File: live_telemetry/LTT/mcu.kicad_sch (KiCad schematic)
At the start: 15 parts, among them J1 Programming Header, U1 MC2562, U2 PIC18F26K83, Y1 Crystal

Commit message: started schematic
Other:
- note added: "CAN"
- note added: "Crystal"
- note added: "MCU"
- note added: "Programmable Test LED's"
- note added: "Programming Header"
- note added: "Standard Waterloo Rocketry PIC18 Setup"
- moved on the sheet: C1, C2, C3, C4, D1, D2, D3, J1, R3, R4, R5, R6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

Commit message: completed schematic
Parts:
- renumbered C4 to C2, C2 to C3, C3 to C4, R3 to R1, R4 to R2, R5 to R3, R6 to R4
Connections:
- net SCLK: now reaches U2.14 (RC3)
- net MOSI: now reaches U2.15 (RC4)
- net MISO: now reaches U2.16 (RC5)
- net RESET: now reaches U2.18 (RC7)
- net CURR_AMP_CAN: now reaches U2.2 (RA0)
- net CS: now reaches U2.7 (RA5)
- no-connect marks 4 -> 9
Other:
- note removed: "MCU"
- moved on the sheet: C2, R1, U2

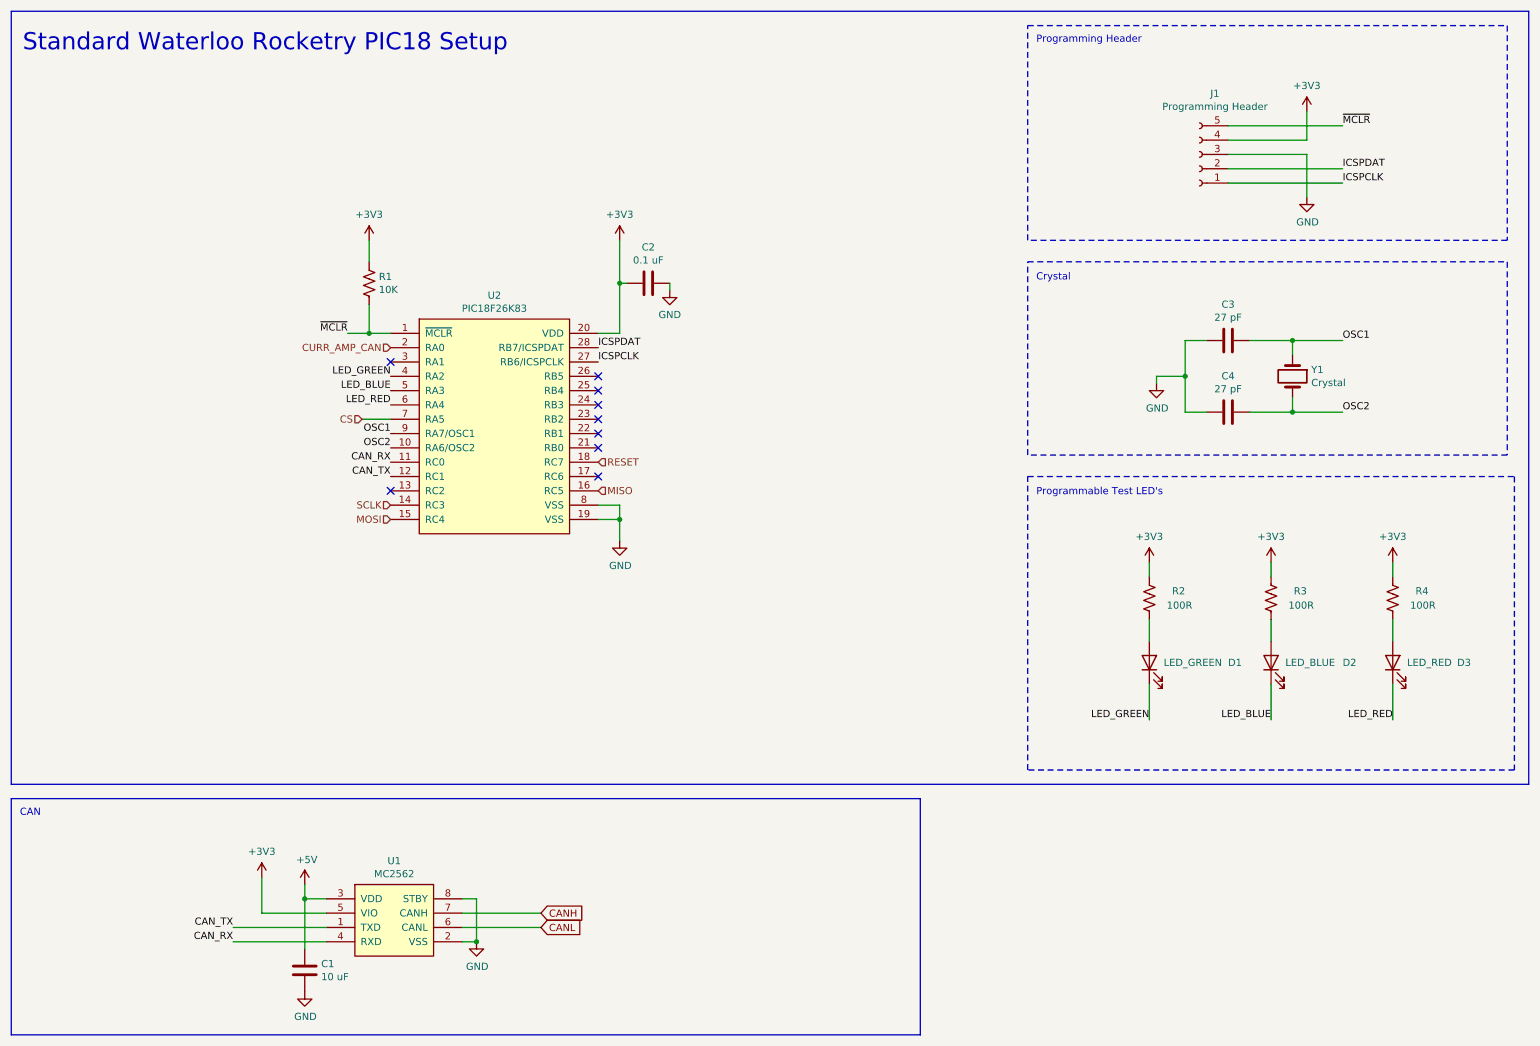
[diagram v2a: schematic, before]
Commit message: switched pic and test led's to 5v from 3v
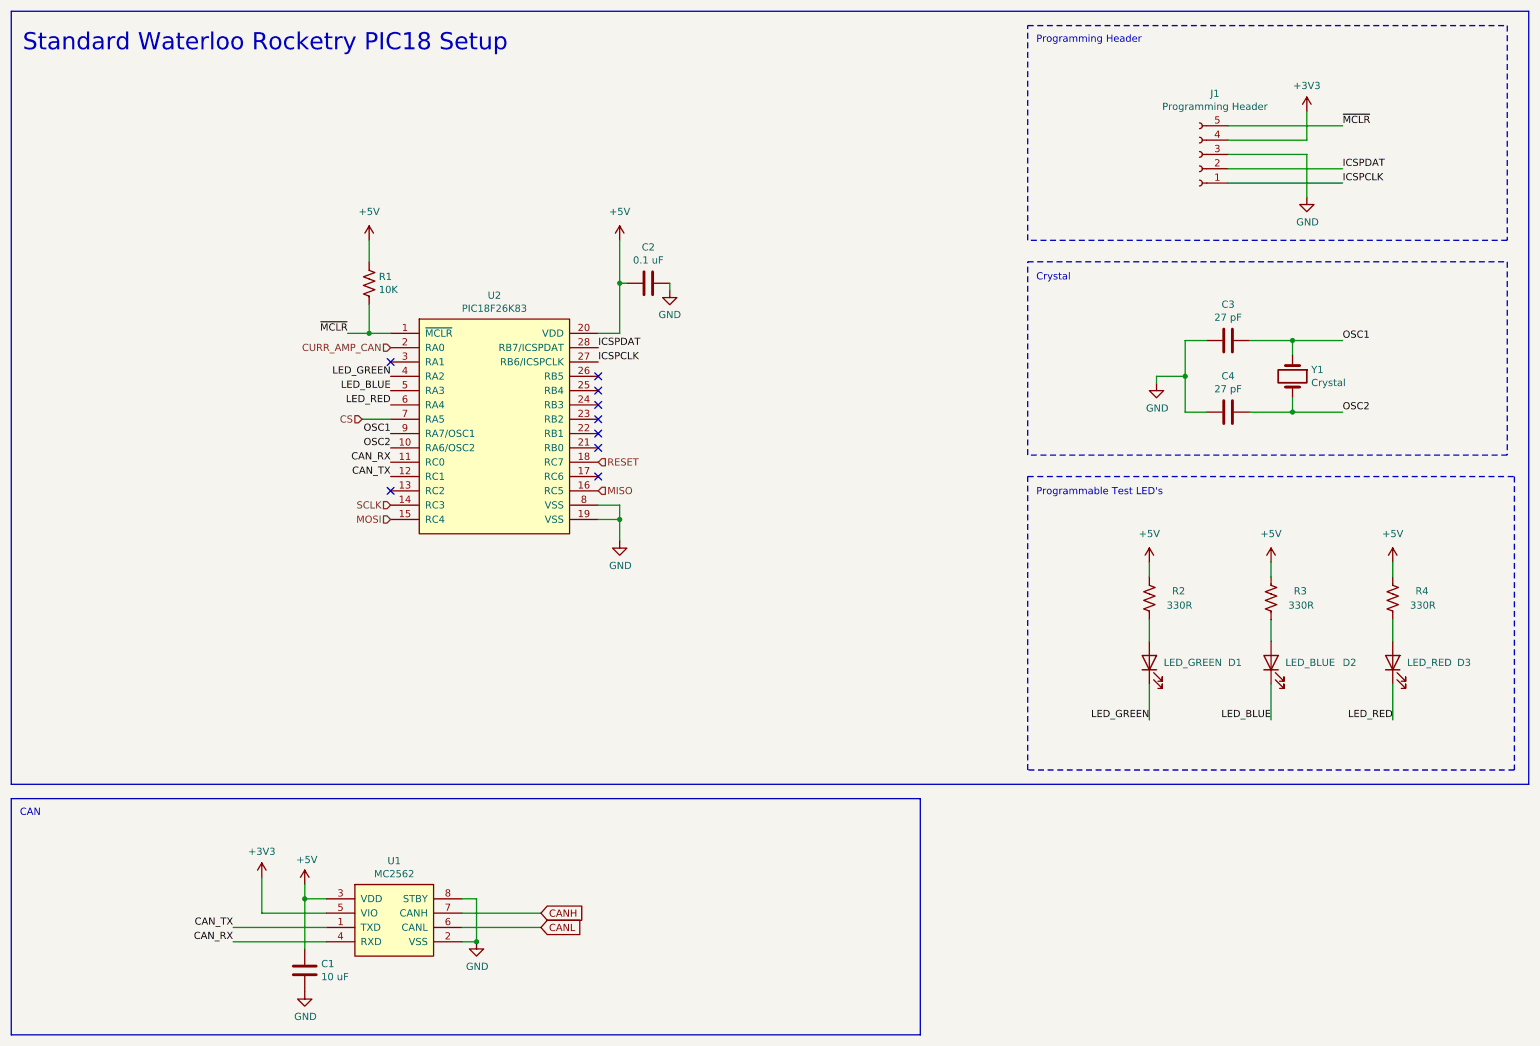
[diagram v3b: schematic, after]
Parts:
- R2, R3, R4: value 100R -> 330R
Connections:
- net +3V3: no longer C2.2, R1.1, R2.2, R3.2, R4.2, U2.20 (VDD)
- net +5V: now also C2.2, R1.1, R2.2, R3.2, R4.2, U2.20 (VDD)

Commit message: implemented comments, added footprints
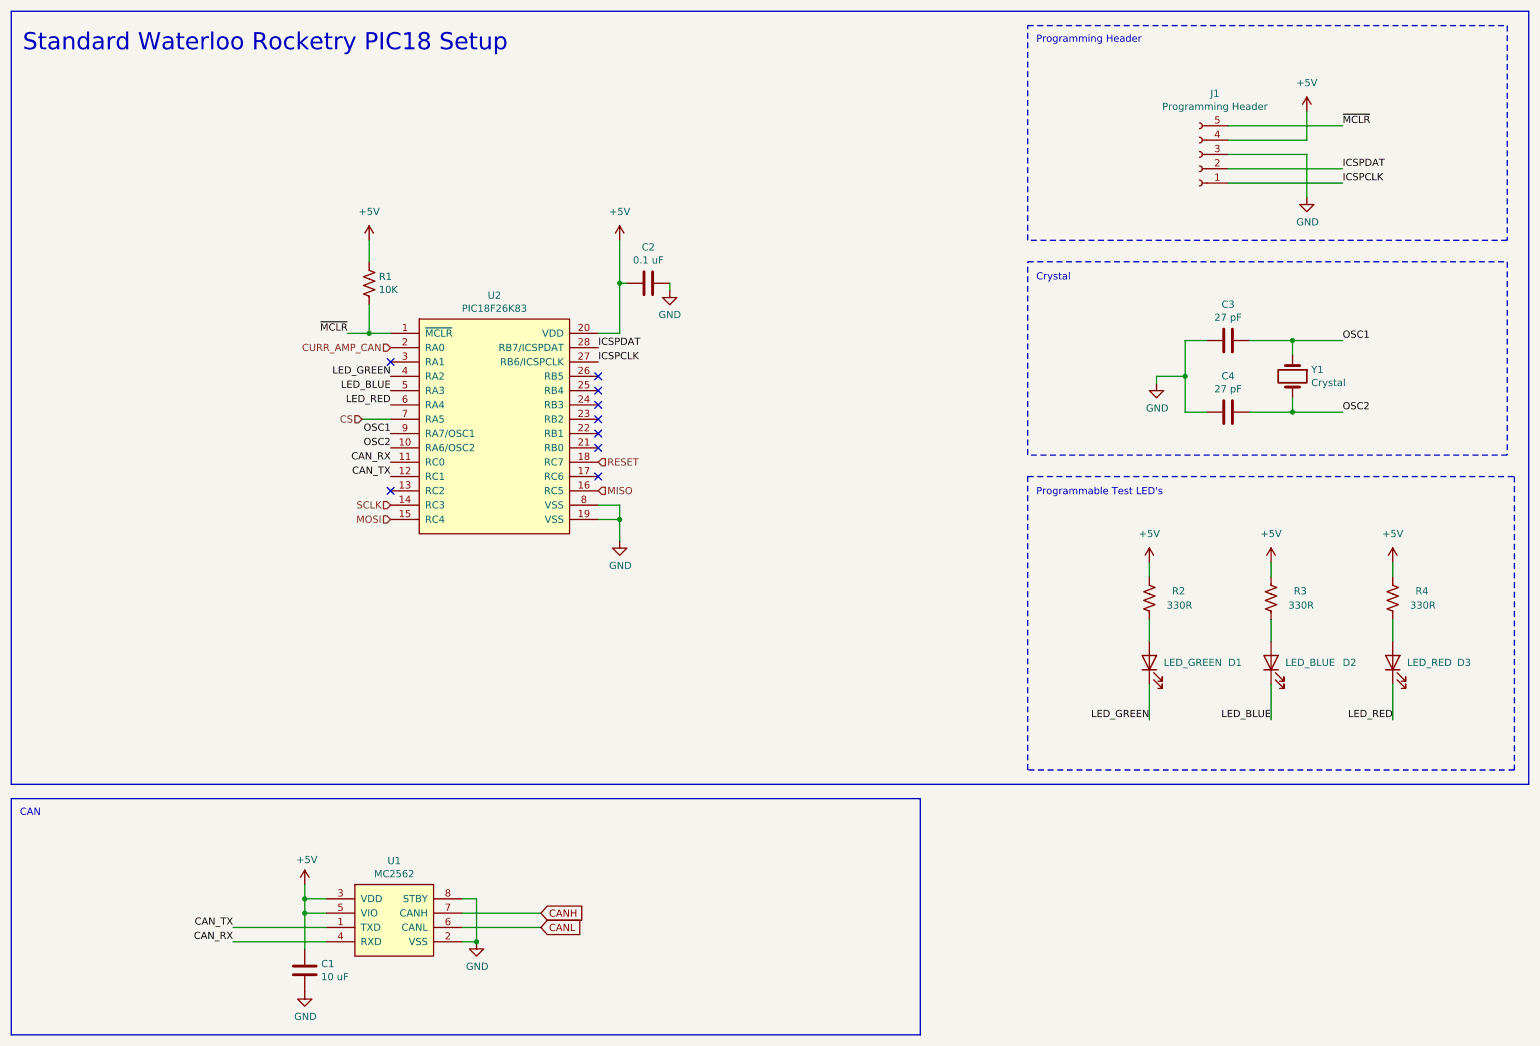
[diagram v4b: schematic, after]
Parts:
- J1: footprint canhw_footprints:PinHeader_5x2.54_SMD_90deg_952-3198-1-ND -> canhw_footprints:PinSocket_5x2.54_SMD_90deg_952-3198-1-ND
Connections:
- net +3V3 is gone; now on net +5V: J1.4 (Pin_4), U1.5 (VIO)
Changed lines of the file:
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@@
+	)
+	(junction
+		(at 66.04 173.99)
+		(diameter 0)
+		(color 0 0 0 0)
 	)
 	(junction
@@
 	(wire
 		(pts
+			(xy 66.04 173.99) (xy 66.04 180.34)
+		)
+		(stroke
+			(width 0)
+			(type default)
+		)
+	)
+	(wire
+		(pts
 			(xy 229.87 39.37) (xy 243.84 39.37)
 		)
@@
 	(wire
 		(pts
-			(xy 58.42 173.99) (xy 69.85 173.99)
-		)
-		(stroke
-			(width 0)
-			(type default)
-		)
-	)
-	(wire
-		(pts
 			(xy 77.47 54.61) (xy 77.47 58.42)
 		)
@@
 	(wire
 		(pts
+			(xy 66.04 173.99) (xy 69.85 173.99)
+		)
+		(stroke
+			(width 0)
+			(type default)
+		)
+	)
+	(wire
+		(pts
 			(xy 241.3 85.09) (xy 241.3 82.55)
 		)
@@
 	(wire
 		(pts
-			(xy 58.42 167.64) (xy 58.42 173.99)
-		)
-		(stroke
-			(width 0)
-			(type default)
-		)
-	)
-	(wire
-		(pts
 			(xy 76.2 86.36) (xy 81.28 86.36)
 		)
@@
 	(wire
 		(pts
-			(xy 66.04 171.45) (xy 66.04 180.34)
+			(xy 66.04 171.45) (xy 66.04 173.99)
 		)
 		(stroke
@@
 	)
 	(symbol
-		(lib_name "+3V3_1")
-		(lib_id "power:+3V3")
-		(at 243.84 31.75 0)
-		(unit 1)
-		(exclude_from_sim no)
-		(in_bom yes)
-		(on_board yes)
-		(dnp no)
-		(property "Reference" "#PWR012"
-			(at 243.84 35.56 0)
-			(effects
-				(font
-					(size 1.27 1.27)
-				)
-				(hide yes)
-			)
-		)
-		(property "Value" "+3V3"
-			(at 243.84 27.178 0)
-			(effects
-				(font
-					(size 1.27 1.27)
-				)
-			)
-		)
-		(property "Footprint" ""
-			(at 243.84 31.75 0)
-			(effects
-				(font
-					(size 1.27 1.27)
-				)
-				(hide yes)
-			)
-		)
-		(property "Datasheet" ""
-			(at 243.84 31.75 0)
-			(effects
-				(font
-					(size 1.27 1.27)
-				)
-				(hide yes)
-			)
-		)
-		(property "Description" ""
-			(at 243.84 31.75 0)
-			(effects
-				(font
-					(size 1.27 1.27)
-				)
-				(hide yes)
-			)
-		)
-		(pin "1"
-		)
-		(instances
-			(project "LTT"
-				(path "/dba0825d-f4bc-4750-857e-1e3e550de350/deb1315d-c738-4804-b21b-d33bc6e28c3c"
-					(reference "#PWR012")
-					(unit 1)
-				)
-			)
-		)
-	)
-	(symbol
 		(lib_id "Device:R_US")
 		(at 237.49 118.11 180)
@@
 	)
 	(symbol
+		(lib_name "+5V_6")
+		(lib_id "power:+5V")
+		(at 243.84 31.75 0)
+		(unit 1)
+		(exclude_from_sim no)
+		(in_bom yes)
+		(on_board yes)
+		(dnp no)
+		(fields_autoplaced yes)
+		(property "Reference" "#PWR012"
+			(at 243.84 35.56 0)
+			(effects
+				(font
+					(size 1.27 1.27)
+				)
+				(hide yes)
+			)
+		)
+		(property "Value" "+5V"
+			(at 243.84 26.67 0)
+			(effects
+				(font
+					(size 1.27 1.27)
+				)
+			)
+		)
+		(property "Footprint" ""
+			(at 243.84 31.75 0)
+			(effects
+				(font
+					(size 1.27 1.27)
+				)
+				(hide yes)
+			)
+		)
+		(property "Datasheet" ""
+			(at 243.84 31.75 0)
+			(effects
+				(font
+					(size 1.27 1.27)
+				)
+				(hide yes)
+			)
+		)
+		(property "Description" "Power symbol creates a global label with name \"+5V\""
+			(at 243.84 31.75 0)
+			(effects
+				(font
+					(size 1.27 1.27)
+				)
+				(hide yes)
+			)
+		)
+		(pin "1"
+		)
+		(instances
+			(project ""
+				(path "/dba0825d-f4bc-4750-857e-1e3e550de350/deb1315d-c738-4804-b21b-d33bc6e28c3c"
+					(reference "#PWR012")
+					(unit 1)
+				)
+			)
+		)
+	)
+	(symbol
 		(lib_id "power:GND")
 		(at 130.81 63.5 0)
@@
 	)
 	(symbol
-		(lib_name "+3V3_1")
-		(lib_id "power:+3V3")
-		(at 58.42 167.64 0)
-		(unit 1)
-		(exclude_from_sim no)
-		(in_bom yes)
-		(on_board yes)
-		(dnp no)
-		(property "Reference" "#PWR01"
-			(at 58.42 171.45 0)
-			(effects
-				(font
-					(size 1.27 1.27)
-				)
-				(hide yes)
-			)
-		)
-		(property "Value" "+3V3"
-			(at 58.42 163.068 0)
-			(effects
-				(font
-					(size 1.27 1.27)
-				)
-			)
-		)
-		(property "Footprint" ""
-			(at 58.42 167.64 0)
-			(effects
-				(font
-					(size 1.27 1.27)
-				)
-				(hide yes)
-			)
-		)
-		(property "Datasheet" ""
-			(at 58.42 167.64 0)
-			(effects
-				(font
-					(size 1.27 1.27)
-				)
-				(hide yes)
-			)
-		)
-		(property "Description" ""
-			(at 58.42 167.64 0)
-			(effects
-				(font
-					(size 1.27 1.27)
-				)
-				(hide yes)
-			)
-		)
-		(pin "1"
-		)
-		(instances
-			(project "LTT"
-				(path "/dba0825d-f4bc-4750-857e-1e3e550de350/deb1315d-c738-4804-b21b-d33bc6e28c3c"
-					(reference "#PWR01")
-					(unit 1)
-				)
-			)
-		)
-	)
-	(symbol
 		(lib_name "+5V_3")
 		(lib_id "power:+5V")
@@
 			)
 		)
-		(property "Footprint" "canhw_footprints:PinHeader_5x2.54_SMD_90deg_952-3198-1-ND"
+		(property "Footprint" "canhw_footprints:PinSocket_5x2.54_SMD_90deg_952-3198-1-ND"
 			(at 224.79 39.37 0)
 			(effects

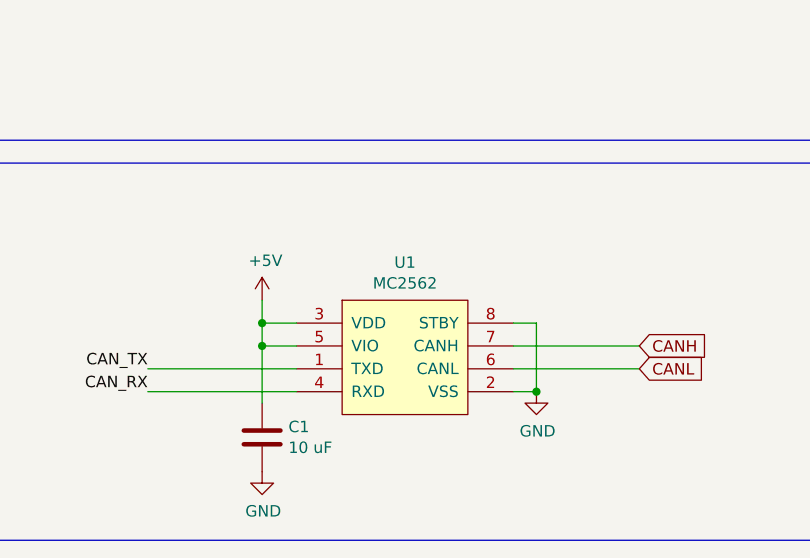
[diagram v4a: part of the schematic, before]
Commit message: initial layout structure
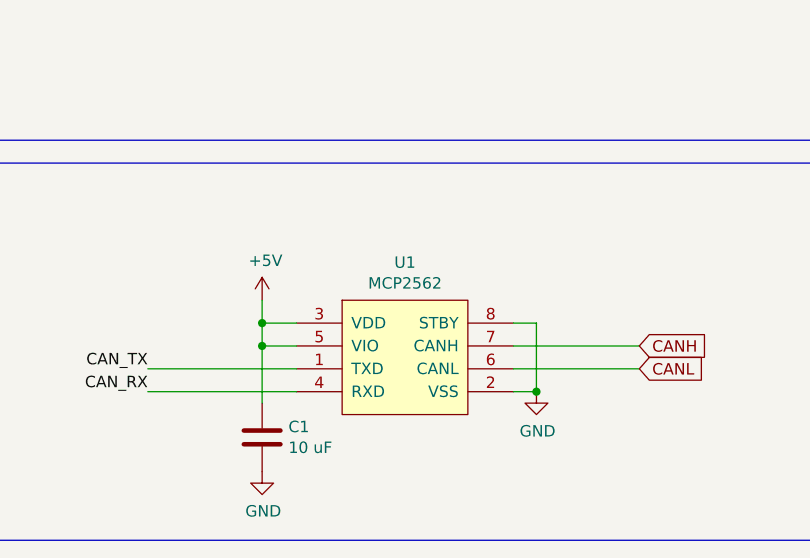
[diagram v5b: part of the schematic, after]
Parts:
- U1: value MC2562 -> MCP2562
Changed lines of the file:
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@@
 		(dnp no)
 		(fields_autoplaced yes)
-		(property "Reference" "#PWR011"
+		(property "Reference" "#PWR010"
 			(at 237.49 115.57 0)
 			(effects
@@
 			(project ""
 				(path "/dba0825d-f4bc-4750-857e-1e3e550de350/deb1315d-c738-4804-b21b-d33bc6e28c3c"
-					(reference "#PWR011")
+					(reference "#PWR010")
 					(unit 1)
 				)
@@
 		(on_board yes)
 		(dnp no)
-		(property "Reference" "#PWR03"
+		(property "Reference" "#PWR02"
 			(at 66.04 194.31 0)
 			(effects
@@
 			(project "LTT"
 				(path "/dba0825d-f4bc-4750-857e-1e3e550de350/deb1315d-c738-4804-b21b-d33bc6e28c3c"
-					(reference "#PWR03")
+					(reference "#PWR02")
 					(unit 1)
 				)
@@
 			)
 		)
-		(property "Value" "MC2562"
+		(property "Value" "MCP2562"
 			(at 81.915 167.0304 0)
 			(effects
@@
 		(dnp no)
 		(fields_autoplaced yes)
-		(property "Reference" "#PWR012"
+		(property "Reference" "#PWR011"
 			(at 243.84 35.56 0)
 			(effects
@@
 			(project ""
 				(path "/dba0825d-f4bc-4750-857e-1e3e550de350/deb1315d-c738-4804-b21b-d33bc6e28c3c"
-					(reference "#PWR012")
+					(reference "#PWR011")
 					(unit 1)
 				)
@@
 		(on_board yes)
 		(dnp no)
-		(property "Reference" "#PWR08"
+		(property "Reference" "#PWR07"
 			(at 130.81 69.85 0)
 			(effects
@@
 			(project "LTT"
 				(path "/dba0825d-f4bc-4750-857e-1e3e550de350/deb1315d-c738-4804-b21b-d33bc6e28c3c"
-					(reference "#PWR08")
+					(reference "#PWR07")
 					(unit 1)
 				)
@@
 		(on_board yes)
 		(dnp no)
-		(property "Reference" "#PWR02"
+		(property "Reference" "#PWR01"
 			(at 66.04 172.72 0)
 			(effects
@@
 			(project "LTT"
 				(path "/dba0825d-f4bc-4750-857e-1e3e550de350/deb1315d-c738-4804-b21b-d33bc6e28c3c"
-					(reference "#PWR02")
+					(reference "#PWR01")
 					(unit 1)
 				)
@@
 		(dnp no)
 		(fields_autoplaced yes)
-		(property "Reference" "#PWR014"
+		(property "Reference" "#PWR013"
 			(at 259.08 115.57 0)
 			(effects
@@
 			(project ""
 				(path "/dba0825d-f4bc-4750-857e-1e3e550de350/deb1315d-c738-4804-b21b-d33bc6e28c3c"
-					(reference "#PWR014")
+					(reference "#PWR013")
 					(unit 1)
 				)
@@
 		(dnp no)
 		(fields_autoplaced yes)
-		(property "Reference" "#PWR09"
+		(property "Reference" "#PWR08"
 			(at 215.9 115.57 0)
 			(effects
@@
 			(project ""
 				(path "/dba0825d-f4bc-4750-857e-1e3e550de350/deb1315d-c738-4804-b21b-d33bc6e28c3c"
-					(reference "#PWR09")
+					(reference "#PWR08")
 					(unit 1)
 				)
@@
 		(on_board yes)
 		(dnp no)
-		(property "Reference" "#PWR013"
+		(property "Reference" "#PWR012"
 			(at 243.84 53.34 0)
 			(effects
@@
 			(project "LTT"
 				(path "/dba0825d-f4bc-4750-857e-1e3e550de350/deb1315d-c738-4804-b21b-d33bc6e28c3c"
-					(reference "#PWR013")
+					(reference "#PWR012")
 					(unit 1)
 				)
@@
 		(on_board yes)
 		(dnp no)
-		(property "Reference" "#PWR07"
+		(property "Reference" "#PWR06"
 			(at 121.92 114.3 0)
 			(effects
@@
 			(project "LTT"
 				(path "/dba0825d-f4bc-4750-857e-1e3e550de350/deb1315d-c738-4804-b21b-d33bc6e28c3c"
-					(reference "#PWR07")
+					(reference "#PWR06")
 					(unit 1)
 				)
@@
 		(dnp no)
 		(fields_autoplaced yes)
-		(property "Reference" "#PWR06"
+		(property "Reference" "#PWR05"
 			(at 121.92 58.42 0)
 			(effects
@@
 			(project ""
 				(path "/dba0825d-f4bc-4750-857e-1e3e550de350/deb1315d-c738-4804-b21b-d33bc6e28c3c"
-					(reference "#PWR06")
+					(reference "#PWR05")
 					(unit 1)
 				)
@@
 		(dnp no)
 		(fields_autoplaced yes)
-		(property "Reference" "#PWR04"
+		(property "Reference" "#PWR03"
 			(at 77.47 58.42 0)
 			(effects
@@
 			(project ""
 				(path "/dba0825d-f4bc-4750-857e-1e3e550de350/deb1315d-c738-4804-b21b-d33bc6e28c3c"
-					(reference "#PWR04")
+					(reference "#PWR03")
 					(unit 1)
 				)
@@
 		(on_board yes)
 		(dnp no)
-		(property "Reference" "#PWR010"
+		(property "Reference" "#PWR09"
 			(at 217.17 86.36 0)
 			(effects
@@
 			(project "LTT"
 				(path "/dba0825d-f4bc-4750-857e-1e3e550de350/deb1315d-c738-4804-b21b-d33bc6e28c3c"
-					(reference "#PWR010")
+					(reference "#PWR09")
 					(unit 1)
 				)
@@
 		(on_board yes)
 		(dnp no)
-		(property "Reference" "#PWR05"
+		(property "Reference" "#PWR04"
 			(at 96.52 185.42 0)
 			(effects
@@
 			(project "LTT"
 				(path "/dba0825d-f4bc-4750-857e-1e3e550de350/deb1315d-c738-4804-b21b-d33bc6e28c3c"
-					(reference "#PWR05")
-					(unit 1)
-				)
+					(reference "#PWR04")
+					(unit 1)
+				)
